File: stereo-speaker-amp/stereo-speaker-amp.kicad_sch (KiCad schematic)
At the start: 22 parts, among them J1 PWR IN, J2 SPK 1, J3 SPK 2, J4 AUX IN, U1 TDA2822

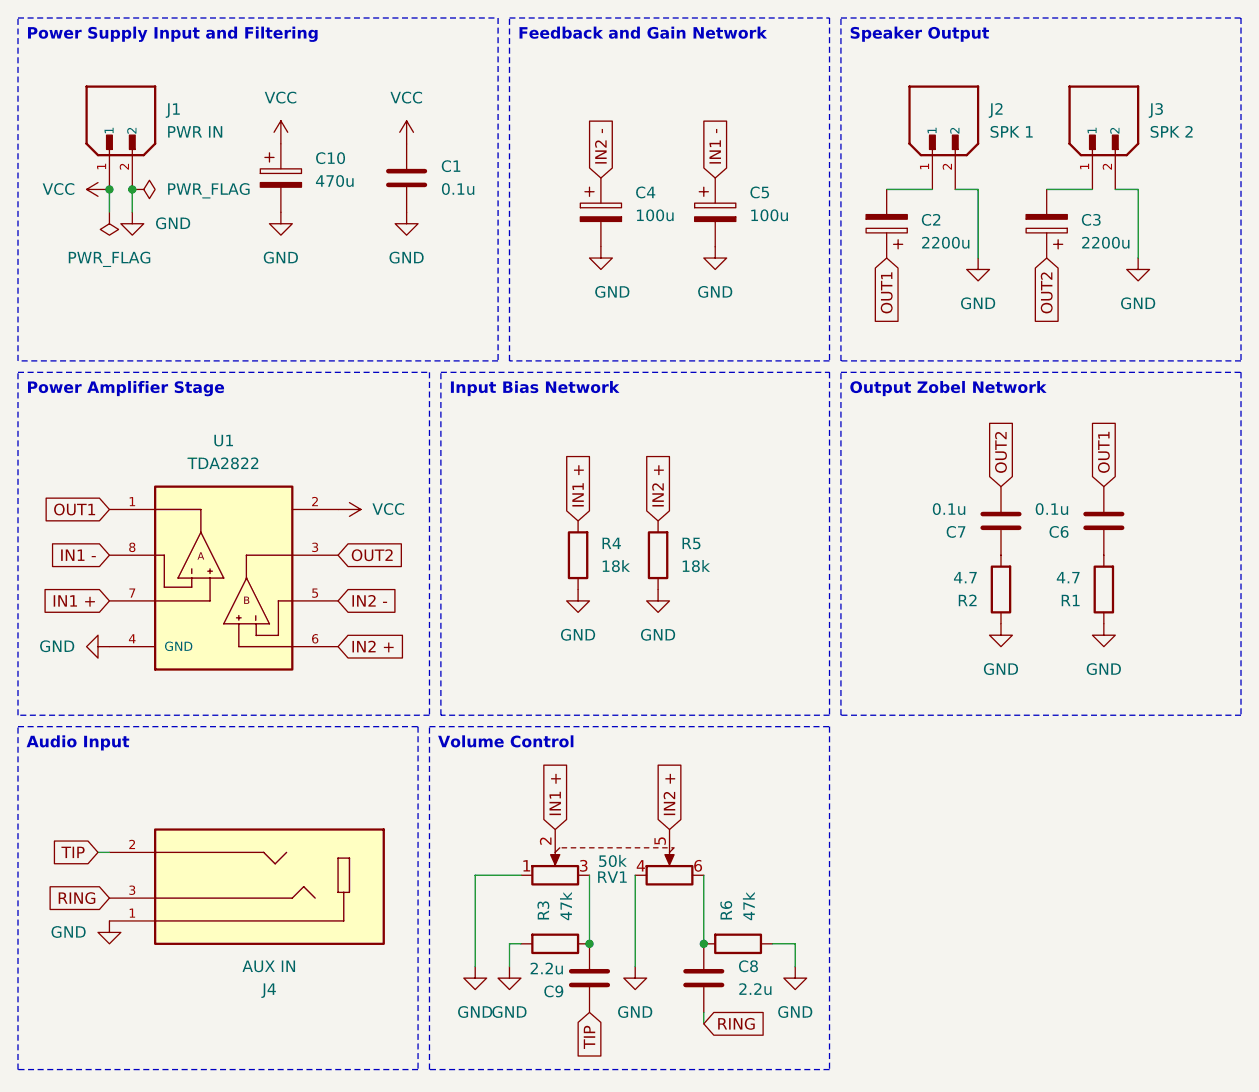
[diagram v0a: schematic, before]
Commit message: Migrate stereo-speaker-amp to KiCad 10 and add self-contained symbol, footprint, and 3D model libraries
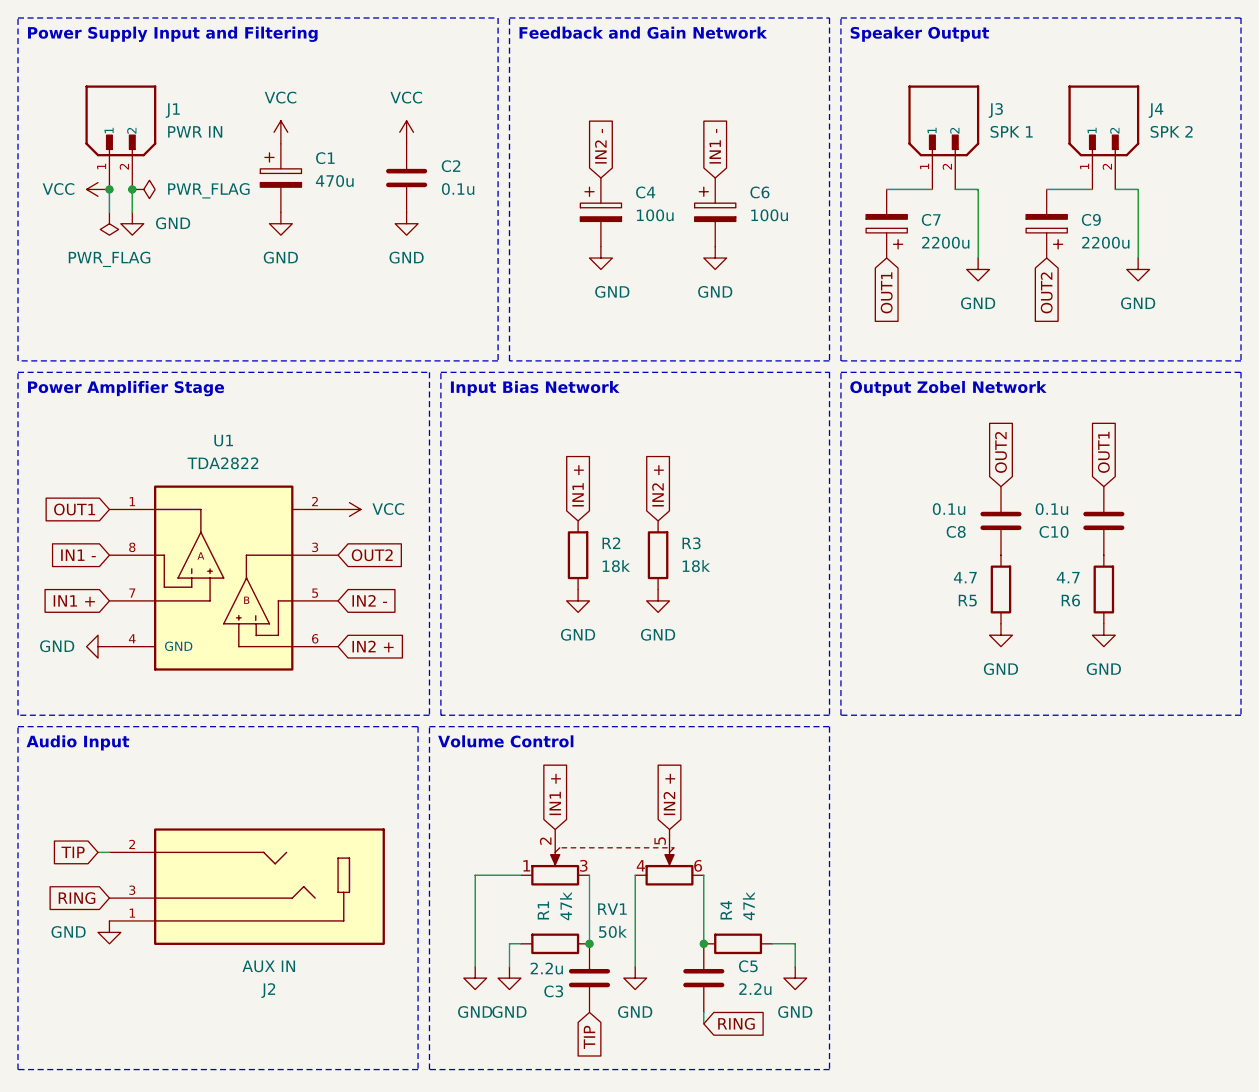
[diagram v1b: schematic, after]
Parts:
- U1: footprint footprints:DIP762W55P254L1092H332Q8N -> footprints:DIP762W45P254L1092H508Q8
- renumbered C10 to C1, C6 to C10, C1 to C2, C9 to C3, C8 to C5, C5 to C6, C2 to C7, C7 to C8, C3 to C9, J4 to J2, J2 to J3, J3 to J4, R3 to R1, R4 to R2, R5 to R3, R6 to R4, R2 to R5, R1 to R6
